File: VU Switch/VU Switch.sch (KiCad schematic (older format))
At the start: 29 parts, among them J1 DC_12V, J10 VU_12V, J11 LED, J12 VU_5V, J13 VU_12V, J2 VU_12V, J3 SELECT, J4 INPUT1, J5 INPUT2, J6 INPUT3, J7 INPUT4, J8 OUTPUT, J9 VU_OUT, K1 HK19F-DC, K2 HK19F-DC, K3 HK19F-DC, K4 HK19F-DC, M1 Mounting_pin, M2 Mounting_pin, M3 Mounting_pin, M4 Mounting_pin, U1 LM7805_TO220

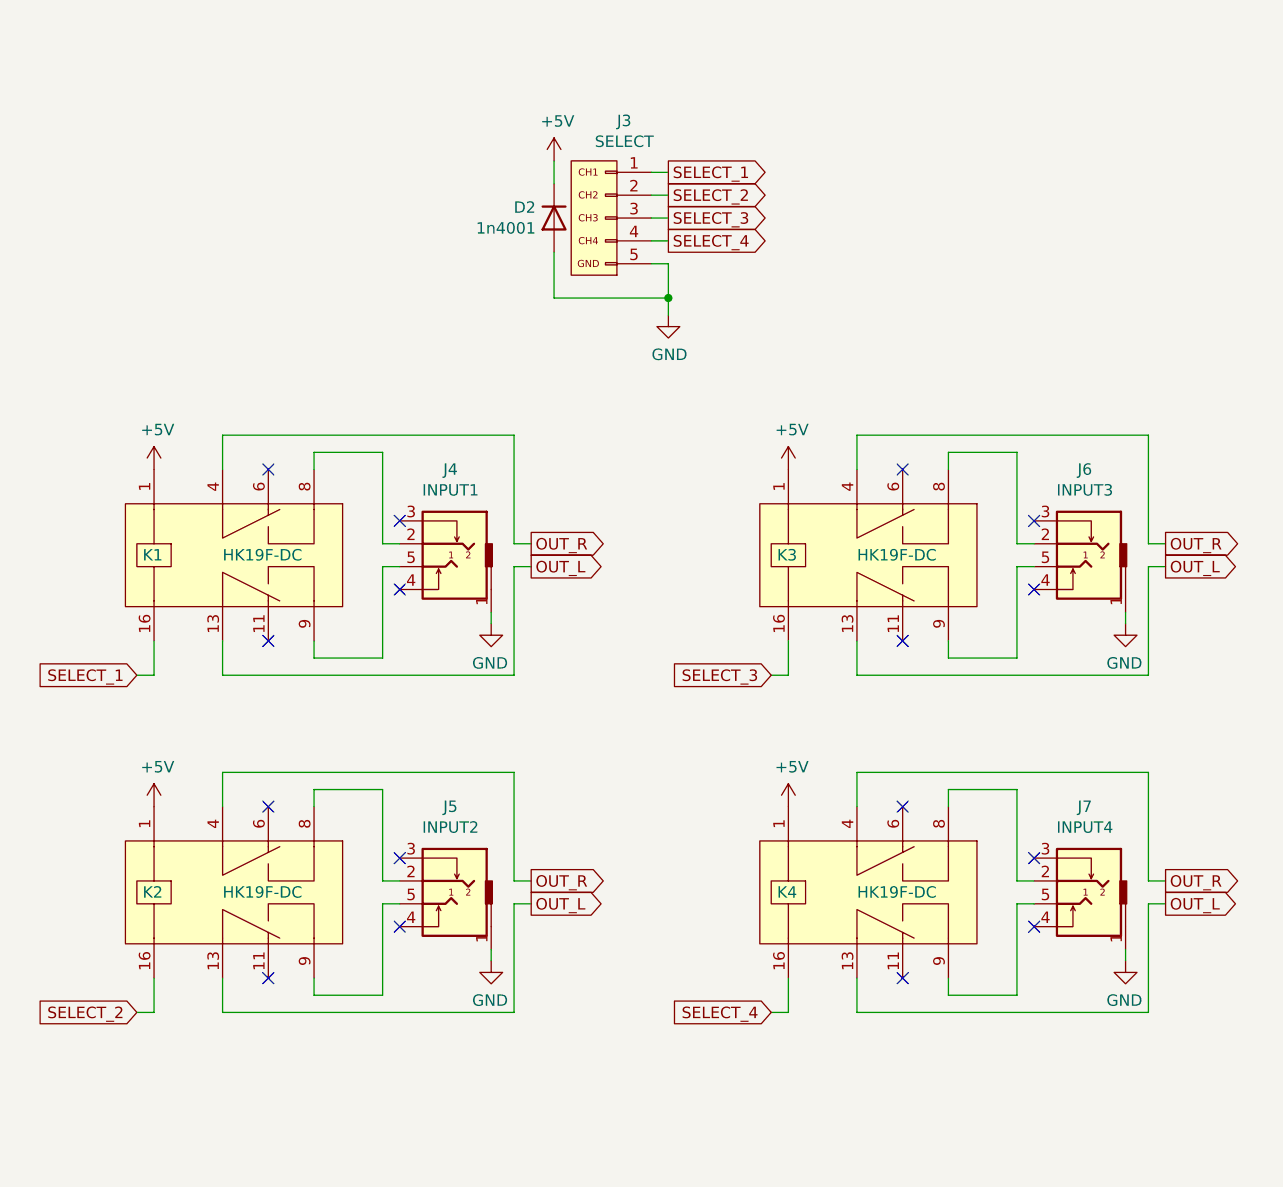
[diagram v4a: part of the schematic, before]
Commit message: Tweaked audio jack position, changed power connector to XH.
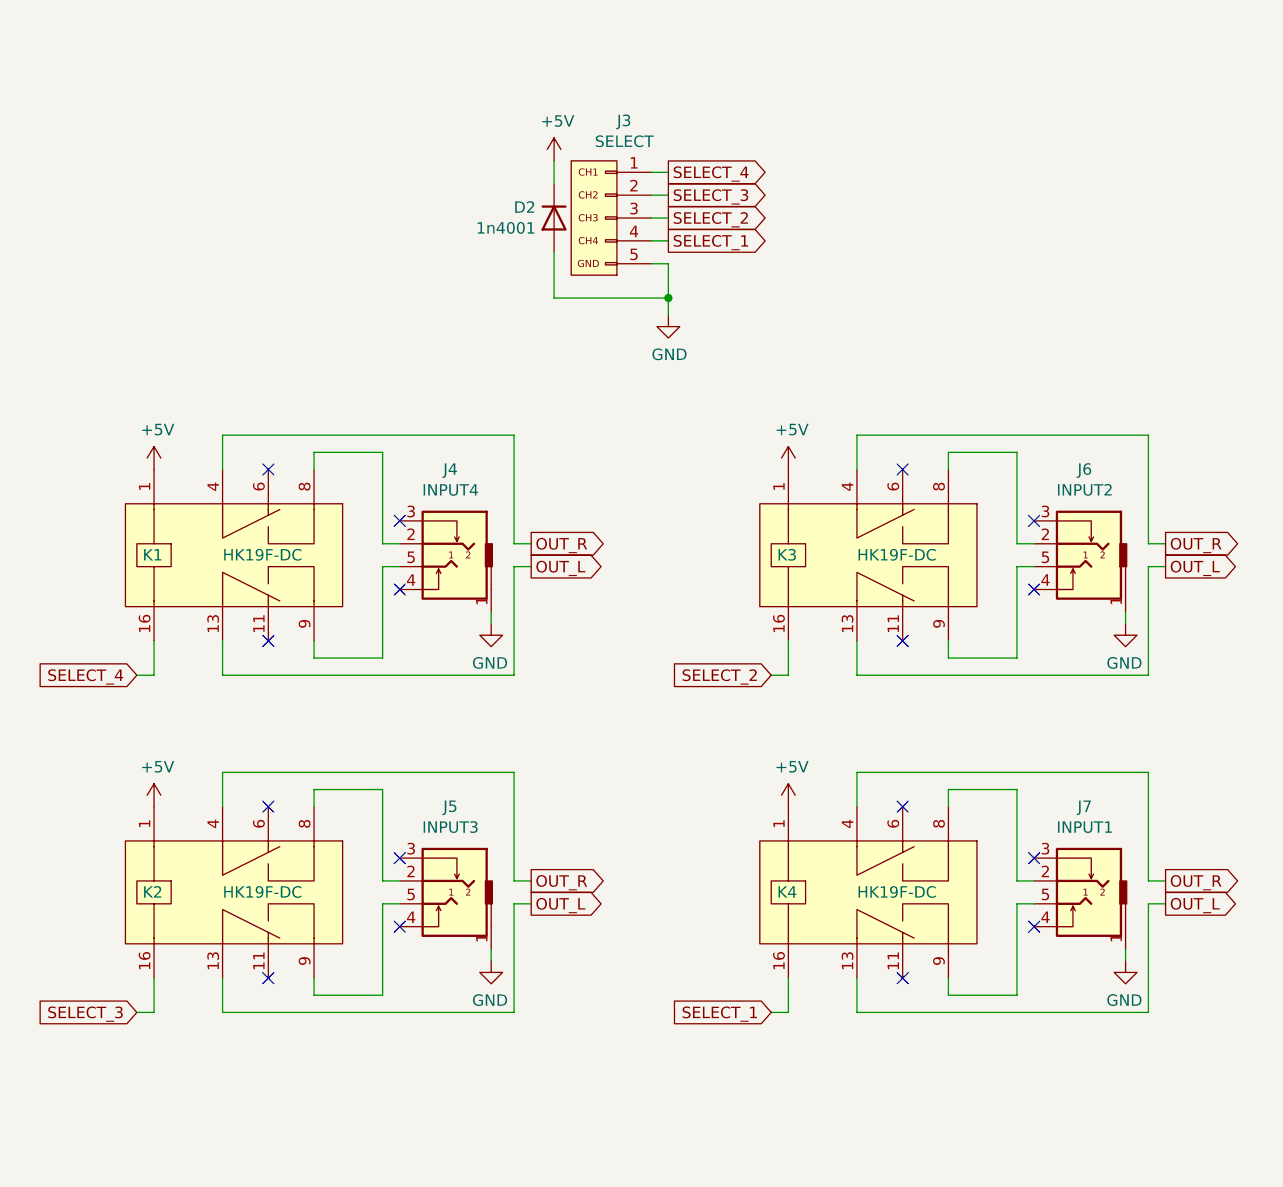
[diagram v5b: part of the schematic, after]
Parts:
- J1: footprint TerminalBlock:TerminalBlock_bornier-2_P5.08mm -> Connector_JST:JST_XH_B2B-XH-A_1x02_P2.50mm_Vertical
- J4: value INPUT1 -> INPUT4
- J5: value INPUT2 -> INPUT3
- J6: value INPUT3 -> INPUT2
- J7: value INPUT4 -> INPUT1
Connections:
- net SELECT_1: now also J3.4 (Pin_4), K4.16; no longer J3.1 (Pin_1), K1.16
- net SELECT_2: now also J3.3 (Pin_3), K3.16; no longer J3.2 (Pin_2), K2.16
- net SELECT_3: now also J3.2 (Pin_2), K2.16; no longer J3.3 (Pin_3), K3.16
- net SELECT_4: now also J3.1 (Pin_1), K1.16; no longer J3.4 (Pin_4), K4.16
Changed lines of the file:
@@
 F 0 "J1" H 2675 7050 50  0000 C CNN
 F 1 "DC_12V" H 2675 6975 50  0000 C CNN
-F 2 "TerminalBlock:TerminalBlock_bornier-2_P5.08mm" H 2700 6850 50  0001 C CNN
+F 2 "Connector_JST:JST_XH_B2B-XH-A_1x02_P2.50mm_Vertical" H 2700 6850 50  0001 C CNN
 F 3 "~" H 2700 6850 50  0001 C CNN
 	1    2700 6850
@@
 NoConn ~ 9325 3025
 $Comp
-L audio_jack:TRS_3.5mm J4
-U 1 1 6008ADA2
-P 3075 2925
-F 0 "J4" H 3053 3350 50  0000 C CNN
-F 1 "INPUT1" H 3053 3259 50  0000 C CNN
-F 2 "audio_jack:Tayda_3.5mm_stereo_TRS_jack_A-853" H 3325 3025 50  0001 C CNN
-F 3 "~" H 3325 3025 50  0001 C CNN
-	1    3075 2925
-	-1   0    0    -1
-$EndComp
-$Comp
 L power:GND #PWR04
 U 1 1 6008ADA8
@@
 NoConn ~ 2875 2725
 NoConn ~ 2875 3025
-$Comp
-L hk19f-dc:HK19F-DC K1
-U 1 1 6009ACF5
-P 1800 2875
-F 0 "K1" H 1750 2875 50  0000 L CNN
-F 1 "HK19F-DC" H 2100 2875 50  0000 L CNN
-F 2 "HK19F-DC:HK19F-DC" H 2650 3000 50  0001 C CNN
-F 3 "" H 2650 3000 50  0001 C CNN
-	1    1800 2875
-	1    0    0    -1
-$EndComp
 $Comp
 L power:+5V #PWR02
@@
 Wire Wire Line
 	3275 3175 3275 3125
-Text GLabel 1725 3400 0    50   Input ~ 0
-SELECT_1
-Text GLabel 4050 1200 2    50   Output ~ 0
-SELECT_1
 Wire Wire Line
 	4050 1200 3975 1200
-Text GLabel 4050 1300 2    50   Output ~ 0
-SELECT_2
 Wire Wire Line
 	4050 1300 3975 1300
-Text GLabel 4050 1400 2    50   Output ~ 0
-SELECT_3
 Wire Wire Line
 	4050 1400 3975 1400
-Text GLabel 4050 1500 2    50   Output ~ 0
-SELECT_4
 Wire Wire Line
 	4050 1500 3975 1500
@@
 P 3075 4400
 F 0 "J5" H 3053 4825 50  0000 C CNN
-F 1 "INPUT2" H 3053 4734 50  0000 C CNN
+F 1 "INPUT3" H 3053 4734 50  0000 C CNN
 F 2 "audio_jack:Tayda_3.5mm_stereo_TRS_jack_A-853" H 3325 4500 50  0001 C CNN
 F 3 "~" H 3325 4500 50  0001 C CNN
@@
 Wire Wire Line
 	3275 4650 3275 4600
-Text GLabel 1725 4875 0    50   Input ~ 0
+Text GLabel 4500 3400 0    50   Input ~ 0
 SELECT_2
 $Comp
@@
 P 5850 2925
 F 0 "J6" H 5828 3350 50  0000 C CNN
-F 1 "INPUT3" H 5828 3259 50  0000 C CNN
+F 1 "INPUT2" H 5828 3259 50  0000 C CNN
 F 2 "audio_jack:Tayda_3.5mm_stereo_TRS_jack_A-853" H 6100 3025 50  0001 C CNN
 F 3 "~" H 6100 3025 50  0001 C CNN
@@
 Wire Wire Line
 	6050 3175 6050 3125
-Text GLabel 4500 3400 0    50   Input ~ 0
+Text GLabel 1725 4875 0    50   Input ~ 0
 SELECT_3
-$Comp
-L audio_jack:TRS_3.5mm J7
-U 1 1 601105C6
-P 5850 4400
-F 0 "J7" H 5828 4825 50  0000 C CNN
-F 1 "INPUT4" H 5828 4734 50  0000 C CNN
-F 2 "audio_jack:Tayda_3.5mm_stereo_TRS_jack_A-853" H 6100 4500 50  0001 C CNN
-F 3 "~" H 6100 4500 50  0001 C CNN
-	1    5850 4400
-	-1   0    0    -1
-$EndComp
 $Comp
 L power:GND #PWR09
@@
 NoConn ~ 5650 4500
 $Comp
-L hk19f-dc:HK19F-DC K4
-U 1 1 601105D4
-P 4575 4350
-F 0 "K4" H 4525 4350 50  0000 L CNN
-F 1 "HK19F-DC" H 4875 4350 50  0000 L CNN
-F 2 "HK19F-DC:HK19F-DC" H 5425 4475 50  0001 C CNN
-F 3 "" H 5425 4475 50  0001 C CNN
-	1    4575 4350
-	1    0    0    -1
-$EndComp
-$Comp
 L power:+5V #PWR07
 U 1 1 601105DA
@@
 Wire Wire Line
 	6050 4650 6050 4600
-Text GLabel 4500 4875 0    50   Input ~ 0
-SELECT_4
 $Comp
 L VU_Switch:VU_OUT J9
@@
 	7950 4175 7950 4325
 Connection ~ 7950 4325
+$Comp
+L audio_jack:TRS_3.5mm J7
+U 1 1 601105C6
+P 5850 4400
+F 0 "J7" H 5828 4825 50  0000 C CNN
+F 1 "INPUT1" H 5828 4734 50  0000 C CNN
+F 2 "audio_jack:Tayda_3.5mm_stereo_TRS_jack_A-853" H 6100 4500 50  0001 C CNN
+F 3 "~" H 6100 4500 50  0001 C CNN
+	1    5850 4400
+	-1   0    0    -1
+$EndComp
+$Comp
+L hk19f-dc:HK19F-DC K4
+U 1 1 601105D4
+P 4575 4350
+F 0 "K4" H 4525 4350 50  0000 L CNN
+F 1 "HK19F-DC" H 4875 4350 50  0000 L CNN
+F 2 "HK19F-DC:HK19F-DC" H 5425 4475 50  0001 C CNN
+F 3 "" H 5425 4475 50  0001 C CNN
+	1    4575 4350
+	1    0    0    -1
+$EndComp
+Text GLabel 1725 3400 0    50   Input ~ 0
+SELECT_4
+Text GLabel 4500 4875 0    50   Input ~ 0
+SELECT_1
+$Comp
+L audio_jack:TRS_3.5mm J4
+U 1 1 6008ADA2
+P 3075 2925
+F 0 "J4" H 3053 3350 50  0000 C CNN
+F 1 "INPUT4" H 3053 3259 50  0000 C CNN
+F 2 "audio_jack:Tayda_3.5mm_stereo_TRS_jack_A-853" H 3325 3025 50  0001 C CNN
+F 3 "~" H 3325 3025 50  0001 C CNN
+	1    3075 2925
+	-1   0    0    -1
+$EndComp
+$Comp
+L hk19f-dc:HK19F-DC K1
+U 1 1 6009ACF5
+P 1800 2875
+F 0 "K1" H 1750 2875 50  0000 L CNN
+F 1 "HK19F-DC" H 2100 2875 50  0000 L CNN
+F 2 "HK19F-DC:HK19F-DC" H 2650 3000 50  0001 C CNN
+F 3 "" H 2650 3000 50  0001 C CNN
+	1    1800 2875
+	1    0    0    -1
+$EndComp
+Text GLabel 4050 1200 2    50   Output ~ 0
+SELECT_4
+Text GLabel 4050 1300 2    50   Output ~ 0
+SELECT_3
+Text GLabel 4050 1400 2    50   Output ~ 0
+SELECT_2
+Text GLabel 4050 1500 2    50   Output ~ 0
+SELECT_1
 $EndSCHEMATC
